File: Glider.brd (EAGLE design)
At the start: 69.1 x 53.3 mm, 37 parts, among them IC1 MCP1700-330, IC2 LM555D, IC3 4050D, Q1 32.768Khz

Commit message: First draft of control board
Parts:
- removed I2C: rtc pins, pinhead:1X02
- removed JP1: sd pins, pinhead:1X04
- removed JP11: led pins, pinhead:1X02
- removed JP12: 3v jumper, jumper:JP1
- removed JP14: (no value), pinhead:1X04
- removed JP2: d8-aref, adafruit:1X08-BIG
- removed JP4: D0-D7, adafruit:1X08-BIG
- removed JP7, JP9: (no value), adafruit:1X06-BIG
- removed LED1: red, adafruit:CHIPLED_0805
- removed LED2: green, adafruit:CHIPLED_0805
- removed R8, R9: (no value), rcl:R0805
- removed U$2: DS1307SO8, SparkFun-FreqCtrl:SO08
- removed U$3: MICROSD, adafruit:MICROSD
- added C6: 15u, rcl:C0805
- added C8: 0.1uF, adafruit:C0805
- added D1: BAS40-04, diode:SOT23
- added IC4: DS1307SO8, SparkFun-FreqCtrl:SO08
- added Q2, Q3: (no value), HAAG:TO252
- added SD: MICROSD, adafruit:MICROSD
- added X1: (no value), con-wago-508:W237-6P
- C5: value (none) -> 10n
- IC1: value MCP1700-330 -> LD6806; device adafruit:TO92 -> AWJLEagleLib:SOT-753
- R3: value 1k -> 10k; device adafruit:R0805 -> rcl:R0805
- R4: value 1k -> 100k; device adafruit:R0805 -> rcl:RTRIM3214W
- moved C3 45.3 mm to (21.0, 44.5)
- moved C1 35.2 mm to (37.5, 6.99), turned to 90 degrees
- moved RESET 31.9 mm to (23.2, 4.88)
- moved R4 30.1 mm to (33.0, 26.0), turned to 270 degrees
- moved LED3 29.1 mm to (24.8, 44.5)
- moved IC1 28.2 mm to (26.7, 29.8)
- moved R5 27.6 mm to (18.4, 32.4), turned to 90 degrees
- moved C5 26.2 mm to (41.9, 22.2), turned to 270 degrees
- moved R6 24.0 mm to (22.9, 44.5), turned to 90 degrees
- moved LED4 23.6 mm to (20.3, 29.8)
- moved C4 22.3 mm to (24.1, 29.8), turned to 270 degrees
- moved SENSOR 22.0 mm to (49.5, 14.6), turned to 180 degrees
- moved R7 18.6 mm to (22.2, 29.8), turned to 270 degrees
- moved IC3 11.4 mm to (24.1, 37.5), turned to 270 degrees
- moved IC2 9.79 mm to (40.0, 26.7), turned to 270 degrees
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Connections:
- removed net 3.3V: JP12.2, JP7.5, U$1.3V
- removed net N$101: JP4.8, U$1.D7
- removed net N$111: JP2.8, U$1.D8
- removed net N$14: LED1.A, R3.1
- removed net N$15: JP7.1, U$1.VIN
- removed net N$154: JP9.1, U$1.A0
- removed net N$164: JP9.2, U$1.A1
- removed net N$17: JP11.2, R3.2
- removed net N$18: LED2.A, R4.2
- removed net N$181: JP9.3, U$1.A2
- removed net N$182: JP9.4, U$1.A3
- removed net N$20: JP11.1, R4.1
- removed net N$87: JP4.1, U$1.D0
- removed net N$88: JP4.2, U$1.D1
- removed net N$89: JP4.3, U$1.D2
- removed net N$90: JP4.4, U$1.D3
- removed net N$98: JP4.5, U$1.D4
- removed net N$99: JP4.6, U$1.D5
- removed net RTC_SCL: I2C.1, JP9.6, R1.2, U$1.A5, U$2.6
- removed net RTC_SDA: I2C.2, JP9.5, R2.2, U$1.A4, U$2.5
- removed net SD_CD: JP14.1, U$3.CD1
- removed net SD_WP: JP14.2
- removed net VDD: U$3.4
- new net 3V: U$1.3V
- new net FLASH: Q2.4, X1.4
- new net I2C_SCL: IC4.6, R1.2, SENSOR.3, U$1.A5
- new net I2C_SDA: IC4.5, R2.2, SENSOR.4, U$1.A4
- new net N$10: C5.1, IC2.5
- new net N$12: IC2.7, Q2.1, R3.1
- new net N$7: D1.1, R4.1
- new net N$8: D1.2, R4.3
- new net N$9: C6.1, D1.3, IC2.2, IC2.6
- new net RELEASE: Q3.4, X1.6
- new net V+: X1.1, X1.3, X1.5
- new net VIN: U$1.VIN
- net +3V3: now also IC1.5, SD.4; no longer IC1.3, JP12.1, JP14.4
- net +5V: now also C8.1, IC1.1, IC1.3, IC2.4, IC4.8, R3.2, SENSOR.5, SENSOR.6; no longer IC1.2, JP7.4, U$2.8
- net GND: now also C5.2, C6.2, C8.2, IC1.2, IC3.11, IC3.14, IC3.9, IC4.4, Q2.3, Q3.3, SD.6, SD.MT1, SD.MT2, SENSOR.1, SENSOR.2, X1.2; no longer IC1.1, JP2.2, JP7.2, JP7.3, LED1.C, LED2.C, U$2.4, U$3.6, U$3.CD2, U$3.MT1
- net MISO: now also SD.7; no longer JP1.1, JP2.4, U$3.7
- net MOSI: now also IC3.5; no longer IC3.3, JP1.2, JP2.5
- net N$1: now also IC4.3; no longer U$2.3
- net N$100: now also Q3.1; no longer JP4.7
- net N$108: no longer JP2.1
- net N$110: no longer JP2.7
- net N$2: now also IC4.1; no longer U$2.1
- net N$3: now also IC4.2; no longer U$2.2
- net N$5: now also IC2.3, R4.2; no longer IC3.9, R5.2
- net RESET: no longer JP7.6
- net SCK: now also IC3.3; no longer IC3.7, JP1.4, JP2.3
- net SD_CS: now also IC3.7, R5.2; no longer JP1.3, JP2.6
- net SD_CSIN: now also IC3.6, SD.2; no longer IC3.10, U$3.2
- net SD_DATAIN: now also IC3.4, SD.3; no longer IC3.2, U$3.3
- net SD_SCKIN: now also IC3.2, SD.5; no longer IC3.6, U$3.5
- net SQW: now also IC4.7; no longer JP14.3, U$2.7
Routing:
- net +5V: track 4.17 -> 108.3 mm, vias 0 -> 5
- net I2C_SCL: track 0.00 -> 72.7 mm
- net I2C_SDA: track 0.00 -> 49.4 mm
- net +3V3: track 0.00 -> 40.1 mm, vias 0 -> 2
- net SD_CS: track 3.76 -> 32.1 mm, vias 0 -> 1
- net MISO: track 3.76 -> 29.9 mm, vias 0 -> 1
- net MOSI: track 3.76 -> 24.7 mm, vias 0 -> 1
- net GND: track 19.9 -> 0.36 mm
- net SCK: track 3.86 -> 20.1 mm, vias 0 -> 2
- net SD_CSIN: track 0.00 -> 15.4 mm
- net SD_DATAIN: track 0.00 -> 15.2 mm
- net SD_SCKIN: track 0.00 -> 14.7 mm
- net N$12: track 0.00 -> 12.2 mm
- net RTC_SCL: track 11.9 -> 0.00 mm
- net N$9: track 0.00 -> 11.8 mm
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- added copper zone on layer 1, net FLASH
- added copper zone on layer 1, net RELEASE
- added copper zone on layer 16, net V+
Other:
- board text removed: "/make/logshield"
- board text removed: "CS"
- board text removed: "DI"
- board text removed: "DO"
- board text removed: "L1"
- board text removed: "L2"
- board text removed: "LEDS"
- board text removed: "SCK"
- board text removed: "SCL"
- board text removed: "SD CARD"
- board text removed: "SDA"
- board text removed: "adafruit"
- board text removed: "make/logshield"
- board text removed: "www.ladyada.net/"

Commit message: First draft layout - to check!
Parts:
- added C7: 0.1uF, adafruit:C0805
- added R8: 10k, rcl:R0805
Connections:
- net +5V: now also C7.1
- net GND: now also C7.2, R8.1
- net N$100: now also R8.2
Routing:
- net I2C_SCL: track 72.7 -> 58.9 mm
- net +5V: track 108.3 -> 117.6 mm
- net N$100: track 13.9 -> 14.5 mm
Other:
- board text added: "HAAG Duke Robotics 2014"
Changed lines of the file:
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@@
 <layer number="37" name="tTest" color="7" fill="1" visible="no" active="yes"/>
 <layer number="38" name="bTest" color="7" fill="1" visible="no" active="yes"/>
-<layer number="39" name="tKeepout" color="4" fill="11" visible="no" active="yes"/>
+<layer number="39" name="tKeepout" color="4" fill="11" visible="yes" active="yes"/>
 <layer number="40" name="bKeepout" color="1" fill="11" visible="no" active="yes"/>
-<layer number="41" name="tRestrict" color="4" fill="10" visible="no" active="yes"/>
+<layer number="41" name="tRestrict" color="4" fill="10" visible="yes" active="yes"/>
 <layer number="42" name="bRestrict" color="1" fill="10" visible="no" active="yes"/>
 <layer number="43" name="vRestrict" color="2" fill="10" visible="no" active="yes"/>
@@
 <wire x1="69.1359" y1="5.0921" x2="69.1359" y2="5.0997" width="0" layer="20"/>
 <circle x="65.5421" y="44.4551" radius="0.8519" width="0.3048" layer="21"/>
+<text x="1.905" y="47.625" size="1.27" layer="25">HAAG
+Duke Robotics 2014</text>
+<wire x1="69.215" y1="6.985" x2="58.42" y2="6.985" width="0.6096" layer="41"/>
+<wire x1="58.42" y1="6.985" x2="58.42" y2="19.05" width="0.6096" layer="41"/>
+<wire x1="58.42" y1="19.05" x2="45.085" y2="19.05" width="0.6096" layer="41"/>
+<wire x1="45.085" y1="19.05" x2="45.085" y2="48.26" width="0.6096" layer="41"/>
 </plain>
 <attributes>
@@
 <attribute name="VALUE" x="33.02" y="23.495" size="1.27" layer="27" rot="R270"/>
 </element>
+<element name="C7" library="adafruit" package="C0805" value="0.1uF" x="21.59" y="19.05" rot="R90"/>
+<element name="R8" library="rcl" package="R0805" value="10k" x="50.165" y="41.275" smashed="yes" rot="R180">
+<attribute name="NAME" x="54.61" y="41.91" size="1.27" layer="25" rot="R180"/>
+<attribute name="VALUE" x="50.8" y="43.815" size="1.27" layer="27" rot="R180"/>
+</element>
 </elements>
 <signals>
@@
 <wire x1="42.605" y1="28.575" x2="42.605" y2="30.105" width="0.4064" layer="1"/>
 <wire x1="42.605" y1="30.105" x2="42.545" y2="30.165" width="0.4064" layer="1"/>
-<wire x1="21.6662" y1="16.637" x2="25.4" y2="16.637" width="0.4064" layer="1"/>
-<wire x1="25.4" y1="16.637" x2="25.908" y2="16.637" width="0.4064" layer="1"/>
+<wire x1="21.6662" y1="16.637" x2="25.908" y2="16.637" width="0.4064" layer="1"/>
 <wire x1="25.908" y1="16.637" x2="26.67" y2="15.875" width="0.4064" layer="1"/>
 <wire x1="26.67" y1="15.875" x2="26.67" y2="14.875" width="0.4064" layer="1"/>
@@
 <wire x1="38.608" y1="2.54" x2="38.608" y2="5.908" width="0.4064" layer="1"/>
 <wire x1="38.608" y1="5.908" x2="38.735" y2="6.035" width="0.4064" layer="1"/>
-<wire x1="46.99" y1="15.875" x2="46.99" y2="13.335" width="0.6096" layer="16"/>
+<wire x1="46.99" y1="15.875" x2="46.99" y2="13.335" width="0.8128" layer="16"/>
 <wire x1="46.99" y1="13.335" x2="46.863" y2="13.335" width="0.6096" layer="16"/>
-<wire x1="46.863" y1="13.335" x2="38.608" y2="5.08" width="0.6096" layer="16"/>
+<wire x1="46.863" y1="13.335" x2="38.608" y2="5.08" width="0.8128" layer="16"/>
 <wire x1="38.608" y1="5.08" x2="38.608" y2="2.54" width="0.6096" layer="16"/>
 <via x="27.94" y="27.305" extent="1-16" drill="0.6"/>
-<via x="25.4" y="16.51" extent="1-16" drill="0.6"/>
 <via x="18.415" y="29.845" extent="1-16" drill="0.6"/>
 <via x="36.83" y="23.495" extent="1-16" drill="0.6"/>
@@
 <wire x1="36.83" y1="16.51" x2="36.83" y2="6.858" width="0.6096" layer="16"/>
 <wire x1="36.83" y1="6.858" x2="38.608" y2="5.08" width="0.6096" layer="16"/>
-<wire x1="25.4" y1="16.51" x2="36.83" y2="16.51" width="0.6096" layer="16"/>
 <wire x1="27.94" y1="27.305" x2="33.02" y2="27.305" width="0.6096" layer="16"/>
 <wire x1="33.02" y1="27.305" x2="36.83" y2="23.495" width="0.6096" layer="16"/>
@@
 <wire x1="27.94" y1="28.275" x2="27.57" y2="28.645" width="0.4064" layer="1"/>
 <wire x1="18.415" y1="31.385" x2="18.415" y2="29.845" width="0.4064" layer="1"/>
-<wire x1="25.4" y1="16.51" x2="25.4" y2="16.637" width="0.4064" layer="1"/>
 <wire x1="36.83" y1="23.495" x2="36.83" y2="24.765" width="0.4064" layer="1"/>
 <wire x1="36.83" y1="24.765" x2="37.405" y2="24.765" width="0.4064" layer="1"/>
 <wire x1="40.64" y1="30.265" x2="39.155" y2="30.265" width="0.4064" layer="1"/>
 <wire x1="39.155" y1="30.265" x2="38.735" y2="29.845" width="0.4064" layer="1"/>
+<contactref element="C7" pad="1"/>
+<via x="19.685" y="16.51" extent="1-16" drill="0.6"/>
+<wire x1="21.6662" y1="16.637" x2="19.812" y2="16.637" width="0.3048" layer="1"/>
+<wire x1="19.812" y1="16.637" x2="19.685" y2="16.51" width="0.3048" layer="1"/>
+<wire x1="21.6662" y1="16.637" x2="21.6662" y2="18.1238" width="0.4064" layer="1"/>
+<wire x1="21.6662" y1="18.1238" x2="21.59" y2="18.2" width="0.3048" layer="1"/>
+<wire x1="36.83" y1="16.51" x2="19.685" y2="16.51" width="0.4064" layer="16"/>
 </signal>
 <signal name="GND">
@@
 <contactref element="SENSOR" pad="1"/>
 <contactref element="SENSOR" pad="2"/>
+<polygon width="0.8128" layer="1" thermals="no">
+<vertex x="62.23" y="16.51"/>
+<vertex x="67.31" y="16.51"/>
+<vertex x="67.31" y="12.7"/>
+<vertex x="62.23" y="12.7"/>
+</polygon>
+<contactref element="C7" pad="2"/>
+<contactref element="R8" pad="1"/>
+<polygon width="0.8128" layer="1" thermals="no">
+<vertex x="45.72" y="24.13"/>
+<vertex x="50.8" y="24.13"/>
+<vertex x="50.8" y="20.32"/>
+<vertex x="45.72" y="20.32"/>
+</polygon>
+<polygon width="0.8128" layer="1" thermals="no">
+<vertex x="45.72" y="34.29"/>
+<vertex x="50.8" y="34.29"/>
+<vertex x="50.8" y="30.48"/>
+<vertex x="45.72" y="30.48"/>
+</polygon>
 </signal>
 <signal name="RESET">
@@
 <wire x1="48.26" y1="14.605" x2="48.26" y2="12.065" width="0.4064" layer="1"/>
 <wire x1="48.26" y1="12.065" x2="47.625" y2="11.43" width="0.4064" layer="1"/>
-<wire x1="47.625" y1="11.43" x2="28.575" y2="11.43" width="0.4064" layer="1"/>
-<wire x1="28.575" y1="11.43" x2="27.94" y2="12.065" width="0.4064" layer="1"/>
-<wire x1="27.94" y1="12.065" x2="27.94" y2="16.51" width="0.4064" layer="1"/>
-<wire x1="27.94" y1="16.51" x2="26.67" y2="17.78" width="0.4064" layer="1"/>
-<wire x1="26.67" y1="17.78" x2="19.05" y2="17.78" width="0.4064" layer="1"/>
-<wire x1="19.05" y1="17.78" x2="18.415" y2="17.145" width="0.4064" layer="1"/>
-<wire x1="18.415" y1="17.145" x2="18.415" y2="15.24" width="0.4064" layer="1"/>
-<wire x1="18.415" y1="15.24" x2="19.685" y2="13.97" width="0.4064" layer="1"/>
-<wire x1="19.685" y1="13.97" x2="21.5392" y2="13.97" width="0.4064" layer="1"/>
+<wire x1="47.625" y1="11.43" x2="25.4" y2="11.43" width="0.4064" layer="1"/>
 <wire x1="21.5392" y1="13.97" x2="21.6662" y2="14.097" width="0.4064" layer="1"/>
+<wire x1="24.4" y1="14.605" x2="25.4" y2="14.605" width="0.4064" layer="1"/>
+<wire x1="25.4" y1="14.605" x2="25.4" y2="11.43" width="0.4064" layer="1"/>
 </signal>
 <signal name="I2C_SDA">
@@
 <contactref element="U$1" pad="D6"/>
 <contactref element="Q3" pad="1"/>
-<wire x1="48.641" y1="50.8" x2="48.641" y2="37.941" width="0.6096" layer="1"/>
+<wire x1="48.641" y1="50.8" x2="48.641" y2="41.275" width="0.6096" layer="1"/>
+<wire x1="48.641" y1="41.275" x2="48.641" y2="37.941" width="0.6096" layer="1"/>
 <wire x1="48.641" y1="37.941" x2="47.905" y2="37.205" width="0.6096" layer="1"/>
+<contactref element="R8" pad="2"/>
+<wire x1="49.215" y1="41.275" x2="48.641" y2="41.275" width="0.6096" layer="1"/>
 </signal>
 <signal name="N$108">
@@
 </board>
 </drawing>
+<compatibility>
+<note version="6.3" minversion="6.2.2" severity="warning">
+Since Version 6.2.2 text objects can contain more than one line,
+which will not be processed correctly with this version.
+</note>
+</compatibility>
 </eagle>

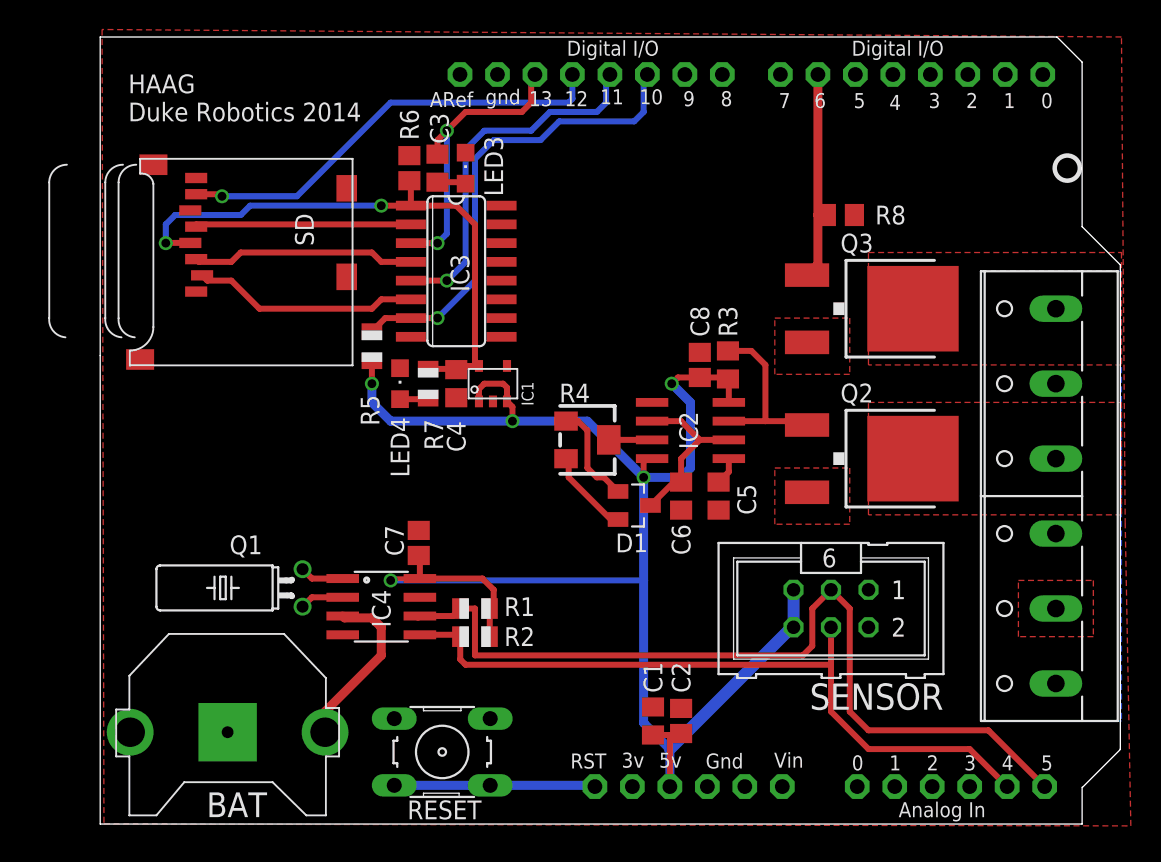
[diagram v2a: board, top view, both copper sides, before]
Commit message: Added accelerometer and barometer with associated level shifters. To be checked!
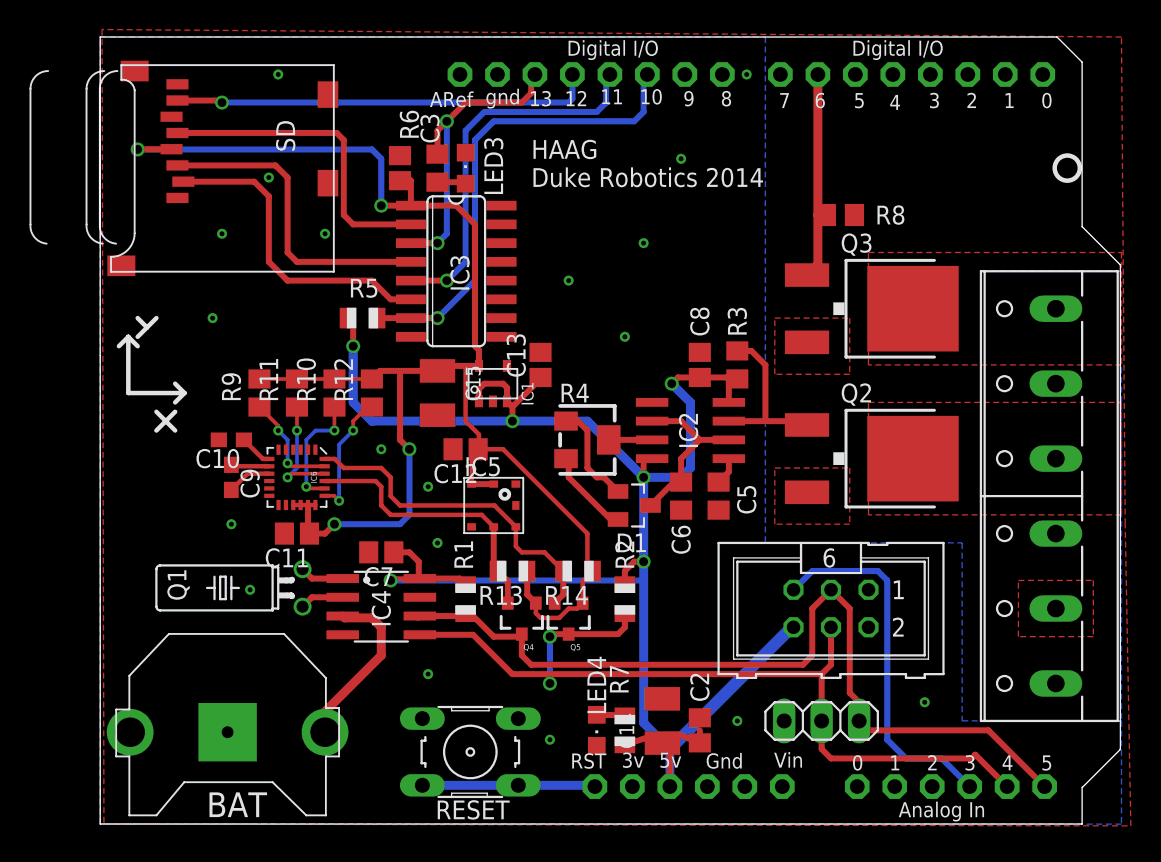
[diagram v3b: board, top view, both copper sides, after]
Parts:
- removed C1, C4: 10uF, rcl:C0805
- added AP: (no value), pinhead:1X03
- added C10: 4u7, rcl:C0603
- added C11, C12, C13: 0.1uF, adafruit:C0805
- added C14, C15: (no value), rcl:SMC_B
- added C9: 220n, rcl:C0603
- added IC5: BMP180, SparkFun-Sensors:BMP180
- added IC6: LSM9DS0, SparkFun-DigitalIC:LGA-24
- added Q4, Q5: MOSFET-NCHANNELBSS123LT1G, SparkFun-DiscreteSemi:SOT23-3
- added R10, R11, R12, R9: 10k, rcl:R0805
- added R13, R14: 4k7, adafruit:R0805
- R1, R2: value 2.2K -> 10k
- moved LED4 27.0 mm to (33.7, 6.35), turned to 180 degrees
- moved R7 27.0 mm to (35.6, 6.35), turned to 90 degrees
- moved R2 10.5 mm to (35.6, 15.2), turned to 270 degrees
- moved SD 6.48 mm to (15.9, 51.4)
- moved C7 2.62 mm to (19.1, 18.4), turned to 180 degrees
- moved R5 2.01 mm to (17.8, 34.3), turned to 0 degrees
- moved RESET 1.90 mm to (25.1, 4.88)
- moved C2 1.42 mm to (40.6, 6.35)
- moved R1 0.90 mm to (24.8, 15.2), turned to 270 degrees
- moved C3 0.63 mm to (20.3, 44.5)
- moved R3 0.63 mm to (43.2, 31.1)
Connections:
- removed net I2C_SCL: IC4.6, R1.2, SENSOR.3, U$1.A5
- removed net I2C_SDA: IC4.5, R2.2, SENSOR.4, U$1.A4
- removed net N$108: U$1.AREF
- removed net N$110: U$1.D9
- new net DHT22: SENSOR.5, U$1.A3
- new net I2C_3V3_SCL: IC5.5, IC6.21, Q4.2, R13.2
- new net I2C_3V3_SDA: IC5.6, IC6.24, Q5.2, R14.2
- new net I2C_5V_SCL: AP.1, IC4.6, Q4.3, R1.2, SENSOR.3, U$1.A5
- new net I2C_5V_SDA: AP.2, IC4.5, Q5.3, R2.2, SENSOR.4, U$1.A4
- new net N$11: IC6.23, R9.1
- new net N$13: IC6.20, R10.1
- new net N$14: IC6.22, R11.1
- new net N$15: IC6.19, R12.1
- new net N$16: C10.1, IC6.7
- new net N$17: C9.1, IC6.8
- new net N$18: C9.2, IC6.9
- net +3V3: now also C11.1, C12.1, C15.+, IC5.2, IC5.3, IC6.15, IC6.16, IC6.17, IC6.18, Q4.1, Q5.1, R10.2, R11.2, R12.2, R13.1, R14.1, R9.2; no longer C4.1, R7.1
- net +5V: now also C13.1, C14.+, R7.1; no longer C1.1, SENSOR.5
- net GND: now also AP.3, C10.2, C11.2, C12.2, C13.2, C14.-, C15.-, IC5.7, IC6.2, IC6.3, IC6.4, IC6.5, IC6.6; no longer C1.2, C4.2
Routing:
- net +3V3: track 40.1 -> 109.1 mm, vias 2 -> 4
- net I2C_5V_SDA: track 0.00 -> 60.7 mm, vias 0 -> 2
- net I2C_SCL: track 58.9 -> 0.00 mm
- net I2C_5V_SCL: track 0.00 -> 58.6 mm
- net I2C_SDA: track 49.4 -> 0.00 mm
- net DHT22: track 0.00 -> 24.8 mm
- net I2C_3V3_SDA: track 0.00 -> 23.6 mm
- net I2C_3V3_SCL: track 0.00 -> 19.1 mm
- net N$15: track 0.00 -> 8.58 mm, vias 0 -> 2
- net N$13: track 0.00 -> 8.22 mm, vias 0 -> 2
- net N$14: track 0.00 -> 7.64 mm, vias 0 -> 2
- net N$11: track 0.00 -> 7.20 mm, vias 0 -> 2
- net SD_SCKIN: track 14.7 -> 21.4 mm
- net +5V: track 117.6 -> 124.0 mm, vias 5 -> 6
- net SD_DATAIN: track 15.2 -> 21.5 mm
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- added copper zone on layer 16, net GND

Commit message: Added DHT22 pullup and tidied up
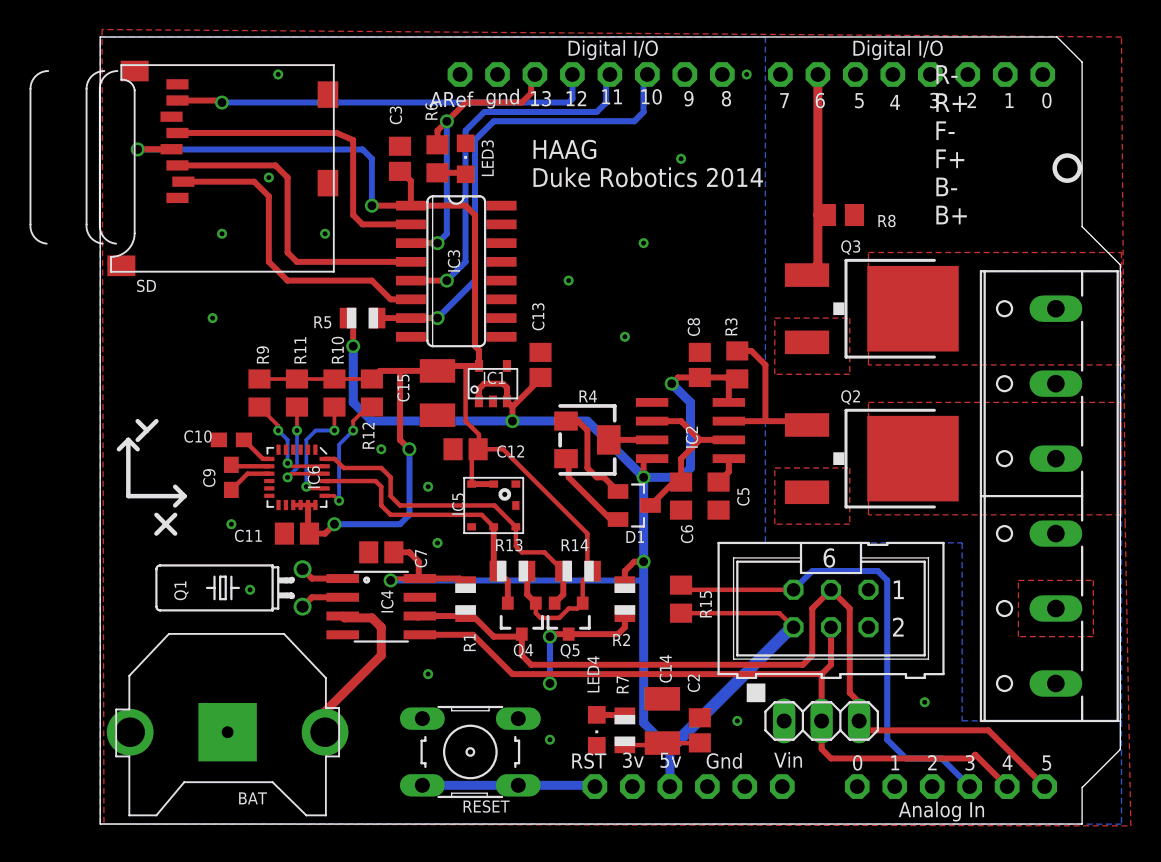
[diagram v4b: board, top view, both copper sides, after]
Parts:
- added R15: 4k7, rcl:R0805
- moved C3 0.63 mm to (20.3, 45.1)
- moved LED3 0.63 mm to (24.8, 45.1)
- moved R6 0.63 mm to (22.9, 45.1)
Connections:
- net +5V: now also R15.2
- net DHT22: now also R15.1
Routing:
- net DHT22: track 24.8 -> 32.8 mm
- net +5V: track 124.0 -> 128.8 mm
- net +3V3: track 109.1 -> 109.8 mm
- net SCK: track 20.7 -> 20.1 mm
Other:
- board text added: "R- R+ F- F+ B- B+"
